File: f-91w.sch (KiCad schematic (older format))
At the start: 41 parts, among them P1 CONN_01X01, P10 CONN_01X01, P11 CONN_01X01, P13 CONN_01X01, P14 CONN_01X01, P2 CONN_01X01, P3 CONN_01X01, P5 CONN_01X01, P6 CONN_01X01, P7 CONN_01X01, P8 CONN_01X01, P9 CONN_01X01, Q1 BC846, U1 CY8C4248LQI-BL483, U2 LCD-F-91W, U3 BME680, Y1 32.768KHz, Y2 24MHz

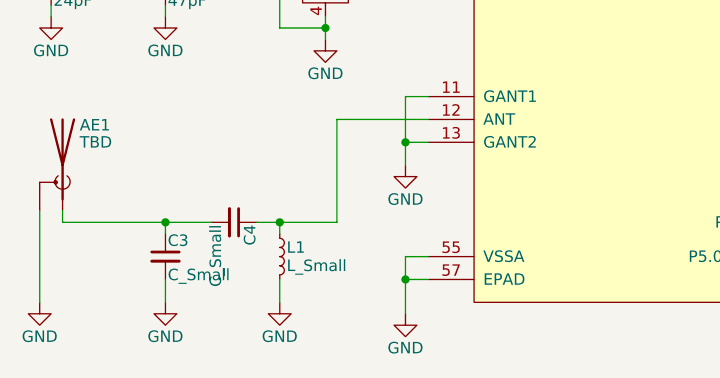
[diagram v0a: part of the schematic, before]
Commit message: Add Johanson 2450AT42E0100 antenna, initial placement
TODO: Proper ground plane and 50R trace
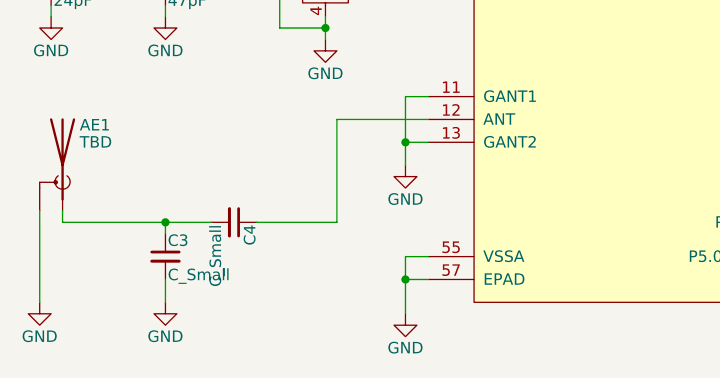
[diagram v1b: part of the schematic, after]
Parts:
- removed L1: L_Small, Resistors_SMD:R_0402, symbol L_Small
- AE1: footprint (none) -> f-91w:2450AT42E0100
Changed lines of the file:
@@
 $EndComp
 $Comp
-L GND #PWR30
+L GND #PWR01
 U 1 1 56EDFDF9
 P 9800 4300
-F 0 "#PWR30" H 9800 4050 50  0001 C CNN
+F 0 "#PWR01" H 9800 4050 50  0001 C CNN
 F 1 "GND" H 9800 4150 50  0000 C CNN
 F 2 "" H 9800 4300 50  0000 C CNN
@@
 $EndComp
 $Comp
-L GND #PWR24
+L GND #PWR02
 U 1 1 56FD3AB4
 P 7000 5050
-F 0 "#PWR24" H 7000 4800 50  0001 C CNN
+F 0 "#PWR02" H 7000 4800 50  0001 C CNN
 F 1 "GND" H 7000 4900 50  0000 C CNN
 F 2 "" H 7000 5050 50  0000 C CNN
@@
 $EndComp
 $Comp
-L VCC #PWR23
+L VCC #PWR03
 U 1 1 570098FF
 P 6550 4550
-F 0 "#PWR23" H 6550 4400 50  0001 C CNN
+F 0 "#PWR03" H 6550 4400 50  0001 C CNN
 F 1 "VCC" H 6550 4700 50  0000 C CNN
 F 2 "" H 6550 4550 50  0000 C CNN
@@
 $EndComp
 $Comp
-L VCC #PWR22
+L VCC #PWR04
 U 1 1 57009B73
 P 6550 4250
-F 0 "#PWR22" H 6550 4100 50  0001 C CNN
+F 0 "#PWR04" H 6550 4100 50  0001 C CNN
 F 1 "VCC" H 6550 4400 50  0000 C CNN
 F 2 "" H 6550 4250 50  0000 C CNN
@@
 B_MODE
 $Comp
-L GND #PWR21
+L GND #PWR05
 U 1 1 5A64BDA3
 P 2750 7550
-F 0 "#PWR21" H 2750 7300 50  0001 C CNN
+F 0 "#PWR05" H 2750 7300 50  0001 C CNN
 F 1 "GND" H 2750 7400 50  0000 C CNN
 F 2 "" H 2750 7550 50  0000 C CNN
@@
 $EndComp
 $Comp
-L GND #PWR20
+L GND #PWR06
 U 1 1 5A64BFB6
 P 2750 6900
-F 0 "#PWR20" H 2750 6650 50  0001 C CNN
+F 0 "#PWR06" H 2750 6650 50  0001 C CNN
 F 1 "GND" H 2750 6750 50  0000 C CNN
 F 2 "" H 2750 6900 50  0000 C CNN
@@
 $EndComp
 $Comp
-L GND #PWR16
+L GND #PWR07
 U 1 1 5A64DCB4
 P 2400 6350
-F 0 "#PWR16" H 2400 6100 50  0001 C CNN
+F 0 "#PWR07" H 2400 6100 50  0001 C CNN
 F 1 "GND" H 2400 6200 50  0000 C CNN
 F 2 "" H 2400 6350 50  0000 C CNN
@@
 $EndComp
 $Comp
-L GND #PWR2
+L GND #PWR08
 U 1 1 5A64E2EF
 P 1200 6250
-F 0 "#PWR2" H 1200 6000 50  0001 C CNN
+F 0 "#PWR08" H 1200 6000 50  0001 C CNN
 F 1 "GND" H 1200 6100 50  0000 C CNN
 F 2 "" H 1200 6250 50  0000 C CNN
@@
 $EndComp
 $Comp
-L GND #PWR6
+L GND #PWR09
 U 1 1 5A64E44A
 P 1700 6250
-F 0 "#PWR6" H 1700 6000 50  0001 C CNN
+F 0 "#PWR09" H 1700 6000 50  0001 C CNN
 F 1 "GND" H 1700 6100 50  0000 C CNN
 F 2 "" H 1700 6250 50  0000 C CNN
@@
 F 0 "AE1" H 1175 7075 50  0000 R CNN
 F 1 "TBD " H 1175 7000 50  0000 R CNN
-F 2 "" H 1250 7000 50  0001 C CNN
+F 2 "f-91w:2450AT42E0100" H 1250 7000 50  0001 C CNN
 F 3 "" H 1250 7000 50  0001 C CNN
 	1    1250 6900
@@
 $EndComp
 $Comp
-L L_Small L1
-U 1 1 5A64F57A
-P 2200 7300
-F 0 "L1" H 2230 7340 50  0000 L CNN
-F 1 "L_Small" H 2230 7260 50  0000 L CNN
-F 2 "Resistors_SMD:R_0402" H 2200 7300 50  0001 C CNN
-F 3 "" H 2200 7300 50  0001 C CNN
-	1    2200 7300
-	1    0    0    -1
-$EndComp
-$Comp
 L C_Small C4
 U 1 1 5A64F666
@@
 $EndComp
 $Comp
-L GND #PWR14
-U 1 1 5A64F863
-P 2200 7500
-F 0 "#PWR14" H 2200 7250 50  0001 C CNN
-F 1 "GND" H 2200 7350 50  0000 C CNN
-F 2 "" H 2200 7500 50  0000 C CNN
-F 3 "" H 2200 7500 50  0000 C CNN
-	1    2200 7500
-	1    0    0    -1
-$EndComp
-$Comp
-L GND #PWR7
+L GND #PWR011
 U 1 1 5A64F8C2
 P 1700 7500
-F 0 "#PWR7" H 1700 7250 50  0001 C CNN
+F 0 "#PWR011" H 1700 7250 50  0001 C CNN
 F 1 "GND" H 1700 7350 50  0000 C CNN
 F 2 "" H 1700 7500 50  0000 C CNN
@@
 $EndComp
 $Comp
-L GND #PWR1
+L GND #PWR012
 U 1 1 5A64FCC4
 P 1150 7500
-F 0 "#PWR1" H 1150 7250 50  0001 C CNN
+F 0 "#PWR012" H 1150 7250 50  0001 C CNN
 F 1 "GND" H 1150 7350 50  0000 C CNN
 F 2 "" H 1150 7500 50  0000 C CNN
@@
 $EndComp
 $Comp
-L GND #PWR15
+L GND #PWR013
 U 1 1 5A650EB4
 P 2250 4650
-F 0 "#PWR15" H 2250 4400 50  0001 C CNN
+F 0 "#PWR013" H 2250 4400 50  0001 C CNN
 F 1 "GND" H 2250 4500 50  0000 C CNN
 F 2 "" H 2250 4650 50  0000 C CNN
@@
 /XRES
 $Comp
-L VDDA #PWR17
+L VDDA #PWR014
 U 1 1 5A652715
 P 2500 3750
-F 0 "#PWR17" H 2500 3600 50  0001 C CNN
+F 0 "#PWR014" H 2500 3600 50  0001 C CNN
 F 1 "VDDA" H 2500 3900 50  0000 C CNN
 F 2 "" H 2500 3750 50  0001 C CNN
@@
 $EndComp
 $Comp
-L GND #PWR28
+L GND #PWR015
 U 1 1 5A6CEE91
 P 8900 1900
-F 0 "#PWR28" H 8900 1650 50  0001 C CNN
+F 0 "#PWR015" H 8900 1650 50  0001 C CNN
 F 1 "GND" H 8900 1750 50  0000 C CNN
 F 2 "" H 8900 1900 50  0000 C CNN
@@
 $EndComp
 $Comp
-L GND #PWR27
+L GND #PWR016
 U 1 1 5A6D0DC3
 P 8550 1900
-F 0 "#PWR27" H 8550 1650 50  0001 C CNN
+F 0 "#PWR016" H 8550 1650 50  0001 C CNN
 F 1 "GND" H 8550 1750 50  0000 C CNN
 F 2 "" H 8550 1900 50  0000 C CNN
@@
 $EndComp
 $Comp
-L GND #PWR26
+L GND #PWR017
 U 1 1 5A6D0E1C
 P 8250 1900
-F 0 "#PWR26" H 8250 1650 50  0001 C CNN
+F 0 "#PWR017" H 8250 1650 50  0001 C CNN
 F 1 "GND" H 8250 1750 50  0000 C CNN
 F 2 "" H 8250 1900 50  0000 C CNN
@@
 $EndComp
 $Comp
-L GND #PWR32
+L GND #PWR018
 U 1 1 5A6D115B
 P 10350 1900
-F 0 "#PWR32" H 10350 1650 50  0001 C CNN
+F 0 "#PWR018" H 10350 1650 50  0001 C CNN
 F 1 "GND" H 10350 1750 50  0000 C CNN
 F 2 "" H 10350 1900 50  0000 C CNN
@@
 SDA
 $Comp
-L VDDD #PWR19
+L VDDD #PWR019
 U 1 1 5A6D21C5
 P 2650 3500
-F 0 "#PWR19" H 2650 3350 50  0001 C CNN
+F 0 "#PWR019" H 2650 3350 50  0001 C CNN
 F 1 "VDDD" H 2650 3650 50  0000 C CNN
 F 2 "" H 2650 3500 50  0001 C CNN
@@
 $EndComp
 $Comp
-L VCC #PWR25
+L VCC #PWR020
 U 1 1 5A6D2B3D
 P 8150 1250
-F 0 "#PWR25" H 8150 1100 50  0001 C CNN
+F 0 "#PWR020" H 8150 1100 50  0001 C CNN
 F 1 "VCC" H 8150 1400 50  0000 C CNN
 F 2 "" H 8150 1250 50  0000 C CNN
@@
 $EndComp
 $Comp
-L VCC #PWR31
+L VCC #PWR021
 U 1 1 5A6D2C66
 P 10350 1250
-F 0 "#PWR31" H 10350 1100 50  0001 C CNN
+F 0 "#PWR021" H 10350 1100 50  0001 C CNN
 F 1 "VCC" H 10350 1400 50  0000 C CNN
 F 2 "" H 10350 1250 50  0000 C CNN
@@
 $EndComp
 $Comp
-L VDDR #PWR18
+L VDDR #PWR022
 U 1 1 5A652763
 P 2500 4050
-F 0 "#PWR18" H 2500 3900 50  0001 C CNN
+F 0 "#PWR022" H 2500 3900 50  0001 C CNN
 F 1 "VDDR" H 2500 4200 50  0000 C CNN
 F 2 "" H 2500 4050 50  0001 C CNN
@@
 $EndComp
 $Comp
-L VDDR #PWR12
+L VDDR #PWR023
 U 1 1 5A6DCCF0
 P 1900 2700
-F 0 "#PWR12" H 1900 2550 50  0001 C CNN
+F 0 "#PWR023" H 1900 2550 50  0001 C CNN
 F 1 "VDDR" H 1900 2850 50  0000 C CNN
 F 2 "" H 1900 2700 50  0001 C CNN
@@
 $EndComp
 $Comp
-L GND #PWR13
+L GND #PWR024
 U 1 1 5A6DCDD7
 P 1900 3300
-F 0 "#PWR13" H 1900 3050 50  0001 C CNN
+F 0 "#PWR024" H 1900 3050 50  0001 C CNN
 F 1 "GND" H 1900 3150 50  0000 C CNN
 F 2 "" H 1900 3300 50  0000 C CNN
@@
 $EndComp
 $Comp
-L VDDA #PWR10
+L VDDA #PWR025
 U 1 1 5A6DE047
 P 1900 1950
-F 0 "#PWR10" H 1900 1800 50  0001 C CNN
+F 0 "#PWR025" H 1900 1800 50  0001 C CNN
 F 1 "VDDA" H 1900 2100 50  0000 C CNN
 F 2 "" H 1900 1950 50  0001 C CNN
@@
 $EndComp
 $Comp
-L VDDD #PWR8
+L VDDD #PWR026
 U 1 1 5A6DE0AF
 P 1900 1150
-F 0 "#PWR8" H 1900 1000 50  0001 C CNN
+F 0 "#PWR026" H 1900 1000 50  0001 C CNN
 F 1 "VDDD" H 1900 1300 50  0000 C CNN
 F 2 "" H 1900 1150 50  0001 C CNN
@@
 $EndComp
 $Comp
-L GND #PWR11
+L GND #PWR027
 U 1 1 5A6DE772
 P 1900 2250
-F 0 "#PWR11" H 1900 2000 50  0001 C CNN
+F 0 "#PWR027" H 1900 2000 50  0001 C CNN
 F 1 "GND" H 1900 2100 50  0000 C CNN
 F 2 "" H 1900 2250 50  0000 C CNN
@@
 $EndComp
 $Comp
-L GND #PWR9
+L GND #PWR028
 U 1 1 5A6DE7EC
 P 1900 1500
-F 0 "#PWR9" H 1900 1250 50  0001 C CNN
+F 0 "#PWR028" H 1900 1250 50  0001 C CNN
 F 1 "GND" H 1900 1350 50  0000 C CNN
 F 2 "" H 1900 1500 50  0000 C CNN
@@
 $EndComp
 $Comp
-L VCC #PWR3
+L VCC #PWR029
 U 1 1 5A6E1864
 P 1450 1100
-F 0 "#PWR3" H 1450 950 50  0001 C CNN
+F 0 "#PWR029" H 1450 950 50  0001 C CNN
 F 1 "VCC" H 1450 1250 50  0000 C CNN
 F 2 "" H 1450 1100 50  0000 C CNN
@@
 $EndComp
 $Comp
-L VCC #PWR4
+L VCC #PWR030
 U 1 1 5A6E1A5B
 P 1450 1900
-F 0 "#PWR4" H 1450 1750 50  0001 C CNN
+F 0 "#PWR030" H 1450 1750 50  0001 C CNN
 F 1 "VCC" H 1450 2050 50  0000 C CNN
 F 2 "" H 1450 1900 50  0000 C CNN
@@
 $EndComp
 $Comp
-L VCC #PWR5
+L VCC #PWR031
 U 1 1 5A6E1C7D
 P 1450 2750
-F 0 "#PWR5" H 1450 2600 50  0001 C CNN
+F 0 "#PWR031" H 1450 2600 50  0001 C CNN
 F 1 "VCC" H 1450 2900 50  0000 C CNN
 F 2 "" H 1450 2750 50  0000 C CNN
@@
 BUZ_EN
 $Comp
-L VCC #PWR29
+L VCC #PWR032
 U 1 1 5A6E93F9
 P 9550 4850
-F 0 "#PWR29" H 9550 4700 50  0001 C CNN
+F 0 "#PWR032" H 9550 4700 50  0001 C CNN
 F 1 "VCC" H 9550 5000 50  0000 C CNN
 F 2 "" H 9550 4850 50  0000 C CNN
@@
 	2450 7150 2100 7150
 Wire Wire Line
-	2200 7150 2200 7200
-Connection ~ 2200 7150
-Wire Wire Line
 	1700 7500 1700 7400
 Wire Wire Line
@@
 	1700 7150 1700 7200
 Wire Wire Line
-	2200 7400 2200 7500
-Wire Wire Line
 	1250 7150 1250 7100

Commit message: Add test points for SWD interface
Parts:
- P1, P2, P3: footprint (none) -> f-91w:TP_1.2mm
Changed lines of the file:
@@
 F 0 "P1" H 8700 5650 50  0000 C CNN
 F 1 "CONN_01X01" H 9000 5550 50  0000 C CNN
-F 2 "" H 8700 5550 50  0001 C CNN
+F 2 "f-91w:TP_1.2mm" H 8700 5550 50  0001 C CNN
 F 3 "" H 8700 5550 50  0000 C CNN
 	1    8700 5550
@@
 F 0 "P2" H 8700 5950 50  0000 C CNN
 F 1 "CONN_01X01" H 9000 5850 50  0000 C CNN
-F 2 "" H 8700 5850 50  0001 C CNN
+F 2 "f-91w:TP_1.2mm" H 8700 5850 50  0001 C CNN
 F 3 "" H 8700 5850 50  0000 C CNN
 	1    8700 5850
@@
 F 0 "P3" H 8700 6250 50  0000 C CNN
 F 1 "CONN_01X01" H 9000 6150 50  0000 C CNN
-F 2 "" H 8700 6150 50  0001 C CNN
+F 2 "f-91w:TP_1.2mm" H 8700 6150 50  0001 C CNN
 F 3 "" H 8700 6150 50  0000 C CNN
 	1    8700 6150

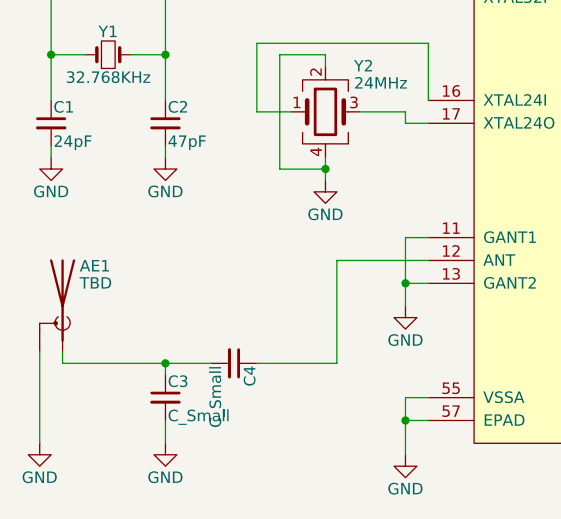
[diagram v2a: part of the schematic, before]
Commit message: Update antenna footprint to add polarity markings
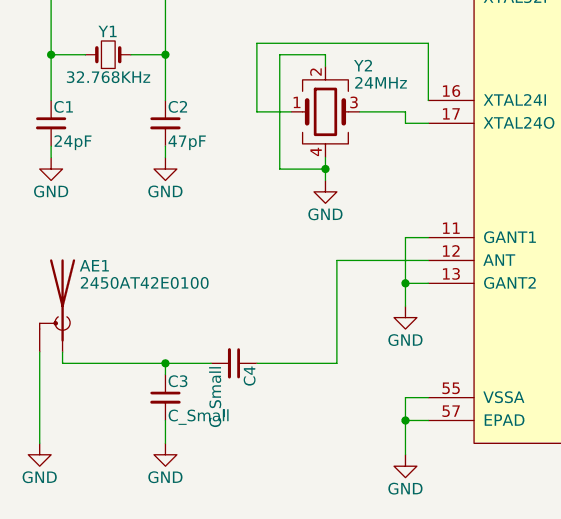
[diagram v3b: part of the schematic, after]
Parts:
- AE1: value TBD -> 2450AT42E0100
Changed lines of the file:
@@
 P 1250 6900
 F 0 "AE1" H 1175 7075 50  0000 R CNN
-F 1 "TBD " H 1175 7000 50  0000 R CNN
+F 1 "2450AT42E0100" H 1175 7000 50  0000 R CNN
 F 2 "f-91w:2450AT42E0100" H 1250 7000 50  0001 C CNN
 F 3 "" H 1250 7000 50  0001 C CNN
@@
 $EndComp
 $Comp
-L GND #PWR011
+L GND #PWR010
 U 1 1 5A64F8C2
 P 1700 7500
-F 0 "#PWR011" H 1700 7250 50  0001 C CNN
+F 0 "#PWR010" H 1700 7250 50  0001 C CNN
 F 1 "GND" H 1700 7350 50  0000 C CNN
 F 2 "" H 1700 7500 50  0000 C CNN
@@
 $EndComp
 $Comp
-L GND #PWR012
+L GND #PWR011
 U 1 1 5A64FCC4
 P 1150 7500
-F 0 "#PWR012" H 1150 7250 50  0001 C CNN
+F 0 "#PWR011" H 1150 7250 50  0001 C CNN
 F 1 "GND" H 1150 7350 50  0000 C CNN
 F 2 "" H 1150 7500 50  0000 C CNN
@@
 $EndComp
 $Comp
-L GND #PWR013
+L GND #PWR012
 U 1 1 5A650EB4
 P 2250 4650
-F 0 "#PWR013" H 2250 4400 50  0001 C CNN
+F 0 "#PWR012" H 2250 4400 50  0001 C CNN
 F 1 "GND" H 2250 4500 50  0000 C CNN
 F 2 "" H 2250 4650 50  0000 C CNN
@@
 /XRES
 $Comp
-L VDDA #PWR014
+L VDDA #PWR013
 U 1 1 5A652715
 P 2500 3750
-F 0 "#PWR014" H 2500 3600 50  0001 C CNN
+F 0 "#PWR013" H 2500 3600 50  0001 C CNN
 F 1 "VDDA" H 2500 3900 50  0000 C CNN
 F 2 "" H 2500 3750 50  0001 C CNN
@@
 $EndComp
 $Comp
-L GND #PWR015
+L GND #PWR014
 U 1 1 5A6CEE91
 P 8900 1900
-F 0 "#PWR015" H 8900 1650 50  0001 C CNN
+F 0 "#PWR014" H 8900 1650 50  0001 C CNN
 F 1 "GND" H 8900 1750 50  0000 C CNN
 F 2 "" H 8900 1900 50  0000 C CNN
@@
 $EndComp
 $Comp
-L GND #PWR016
+L GND #PWR015
 U 1 1 5A6D0DC3
 P 8550 1900
-F 0 "#PWR016" H 8550 1650 50  0001 C CNN
+F 0 "#PWR015" H 8550 1650 50  0001 C CNN
 F 1 "GND" H 8550 1750 50  0000 C CNN
 F 2 "" H 8550 1900 50  0000 C CNN
@@
 $EndComp
 $Comp
-L GND #PWR017
+L GND #PWR016
 U 1 1 5A6D0E1C
 P 8250 1900
-F 0 "#PWR017" H 8250 1650 50  0001 C CNN
+F 0 "#PWR016" H 8250 1650 50  0001 C CNN
 F 1 "GND" H 8250 1750 50  0000 C CNN
 F 2 "" H 8250 1900 50  0000 C CNN
@@
 $EndComp
 $Comp
-L GND #PWR018
+L GND #PWR017
 U 1 1 5A6D115B
 P 10350 1900
-F 0 "#PWR018" H 10350 1650 50  0001 C CNN
+F 0 "#PWR017" H 10350 1650 50  0001 C CNN
 F 1 "GND" H 10350 1750 50  0000 C CNN
 F 2 "" H 10350 1900 50  0000 C CNN
@@
 SDA
 $Comp
-L VDDD #PWR019
+L VDDD #PWR018
 U 1 1 5A6D21C5
 P 2650 3500
-F 0 "#PWR019" H 2650 3350 50  0001 C CNN
+F 0 "#PWR018" H 2650 3350 50  0001 C CNN
 F 1 "VDDD" H 2650 3650 50  0000 C CNN
 F 2 "" H 2650 3500 50  0001 C CNN
@@
 $EndComp
 $Comp
-L VCC #PWR020
+L VCC #PWR019
 U 1 1 5A6D2B3D
 P 8150 1250
-F 0 "#PWR020" H 8150 1100 50  0001 C CNN
+F 0 "#PWR019" H 8150 1100 50  0001 C CNN
 F 1 "VCC" H 8150 1400 50  0000 C CNN
 F 2 "" H 8150 1250 50  0000 C CNN
@@
 $EndComp
 $Comp
-L VCC #PWR021
+L VCC #PWR020
 U 1 1 5A6D2C66
 P 10350 1250
-F 0 "#PWR021" H 10350 1100 50  0001 C CNN
+F 0 "#PWR020" H 10350 1100 50  0001 C CNN
 F 1 "VCC" H 10350 1400 50  0000 C CNN
 F 2 "" H 10350 1250 50  0000 C CNN
@@
 $EndComp
 $Comp
-L VDDR #PWR022
+L VDDR #PWR021
 U 1 1 5A652763
 P 2500 4050
-F 0 "#PWR022" H 2500 3900 50  0001 C CNN
+F 0 "#PWR021" H 2500 3900 50  0001 C CNN
 F 1 "VDDR" H 2500 4200 50  0000 C CNN
 F 2 "" H 2500 4050 50  0001 C CNN
@@
 $EndComp
 $Comp
-L VDDR #PWR023
+L VDDR #PWR022
 U 1 1 5A6DCCF0
 P 1900 2700
-F 0 "#PWR023" H 1900 2550 50  0001 C CNN
+F 0 "#PWR022" H 1900 2550 50  0001 C CNN
 F 1 "VDDR" H 1900 2850 50  0000 C CNN
 F 2 "" H 1900 2700 50  0001 C CNN
@@
 $EndComp
 $Comp
-L GND #PWR024
+L GND #PWR023
 U 1 1 5A6DCDD7
 P 1900 3300
-F 0 "#PWR024" H 1900 3050 50  0001 C CNN
+F 0 "#PWR023" H 1900 3050 50  0001 C CNN
 F 1 "GND" H 1900 3150 50  0000 C CNN
 F 2 "" H 1900 3300 50  0000 C CNN
@@
 $EndComp
 $Comp
-L VDDA #PWR025
+L VDDA #PWR024
 U 1 1 5A6DE047
 P 1900 1950
-F 0 "#PWR025" H 1900 1800 50  0001 C CNN
+F 0 "#PWR024" H 1900 1800 50  0001 C CNN
 F 1 "VDDA" H 1900 2100 50  0000 C CNN
 F 2 "" H 1900 1950 50  0001 C CNN
@@
 $EndComp
 $Comp
-L VDDD #PWR026
+L VDDD #PWR025
 U 1 1 5A6DE0AF
 P 1900 1150
-F 0 "#PWR026" H 1900 1000 50  0001 C CNN
+F 0 "#PWR025" H 1900 1000 50  0001 C CNN
 F 1 "VDDD" H 1900 1300 50  0000 C CNN
 F 2 "" H 1900 1150 50  0001 C CNN
@@
 $EndComp
 $Comp
-L GND #PWR027
+L GND #PWR026
 U 1 1 5A6DE772
 P 1900 2250
-F 0 "#PWR027" H 1900 2000 50  0001 C CNN
+F 0 "#PWR026" H 1900 2000 50  0001 C CNN
 F 1 "GND" H 1900 2100 50  0000 C CNN
 F 2 "" H 1900 2250 50  0000 C CNN
@@
 $EndComp
 $Comp
-L GND #PWR028
+L GND #PWR027
 U 1 1 5A6DE7EC
 P 1900 1500
-F 0 "#PWR028" H 1900 1250 50  0001 C CNN
+F 0 "#PWR027" H 1900 1250 50  0001 C CNN
 F 1 "GND" H 1900 1350 50  0000 C CNN
 F 2 "" H 1900 1500 50  0000 C CNN
@@
 $EndComp
 $Comp
-L VCC #PWR029
+L VCC #PWR028
 U 1 1 5A6E1864
 P 1450 1100
-F 0 "#PWR029" H 1450 950 50  0001 C CNN
+F 0 "#PWR028" H 1450 950 50  0001 C CNN
 F 1 "VCC" H 1450 1250 50  0000 C CNN
 F 2 "" H 1450 1100 50  0000 C CNN
@@
 $EndComp
 $Comp
-L VCC #PWR030
+L VCC #PWR029
 U 1 1 5A6E1A5B
 P 1450 1900
-F 0 "#PWR030" H 1450 1750 50  0001 C CNN
+F 0 "#PWR029" H 1450 1750 50  0001 C CNN
 F 1 "VCC" H 1450 2050 50  0000 C CNN
 F 2 "" H 1450 1900 50  0000 C CNN
@@
 $EndComp
 $Comp
-L VCC #PWR031
+L VCC #PWR030
 U 1 1 5A6E1C7D
 P 1450 2750
-F 0 "#PWR031" H 1450 2600 50  0001 C CNN
+F 0 "#PWR030" H 1450 2600 50  0001 C CNN
 F 1 "VCC" H 1450 2900 50  0000 C CNN
 F 2 "" H 1450 2750 50  0000 C CNN
@@
 BUZ_EN
 $Comp
-L VCC #PWR032
+L VCC #PWR031
 U 1 1 5A6E93F9
 P 9550 4850
-F 0 "#PWR032" H 9550 4700 50  0001 C CNN
+F 0 "#PWR031" H 9550 4700 50  0001 C CNN
 F 1 "VCC" H 9550 5000 50  0000 C CNN
 F 2 "" H 9550 4850 50  0000 C CNN

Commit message: Fix 32KHz crystal footprint for Abracon ABS06 series
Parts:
- Y1: footprint Crystals:Crystal_SMD_TXC_9HT11-2pin_2.0x1.2mm -> f-91w:Crystal_SMD_Abracon_ABS06-2pin_2.0x1.2mm
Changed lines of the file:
@@
 F 0 "Y1" H 1450 5900 50  0000 C CNN
 F 1 "32.768KHz" H 1450 5700 50  0000 C CNN
-F 2 "Crystals:Crystal_SMD_TXC_9HT11-2pin_2.0x1.2mm" H 1450 5800 50  0001 C CNN
+F 2 "f-91w:Crystal_SMD_Abracon_ABS06-2pin_2.0x1.2mm" H 1450 5800 50  0001 C CNN
 F 3 "" H 1450 5800 50  0001 C CNN
 F 4 "ABS06-32.768KHZ-1-T" H 1450 5800 60  0001 C CNN "MPN"

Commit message: Update schematic and project to KiCad 5.0
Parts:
- AE1: symbol Antenna_Shield -> Device:Antenna_Shield
- C1, C10, C11, C12, C13, C14, C15, C16, C17, C18, C2, C3, C4, C5, C6, C7, C8, C9: symbol C_Small -> Device:C_Small
- L4: symbol Ferrite_Bead_Small -> Device:Ferrite_Bead_Small
- P1, P10, P11, P13, P14, P2, P3, P5, P6, P7, P8, P9: symbol Conn_01x01 -> Connector_Generic:Conn_01x01
- Q1: symbol Q_NPN_BEC -> Device:Q_NPN_BEC
- R2, R3: symbol R -> Device:R
- U1: symbol CY8C4248LQI-BL483 -> f-91w:CY8C4248LQI-BL483
- U2: symbol LCD-F-91W -> f-91w:LCD-F-91W
- U3: symbol BME680 -> f-91w:BME680
- Y1: symbol Crystal_Small -> Device:Crystal_Small
- Y2: symbol Crystal_GND24 -> Device:Crystal_GND24

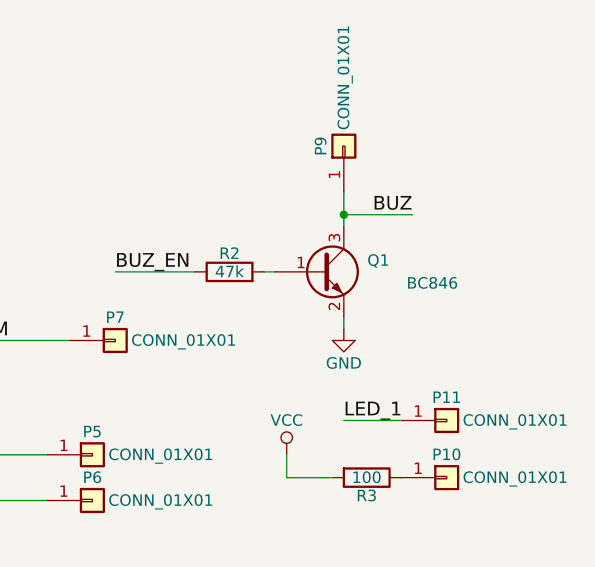
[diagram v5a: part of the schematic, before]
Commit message: Change Q1 from obsolete BC846 to BC847BTT1
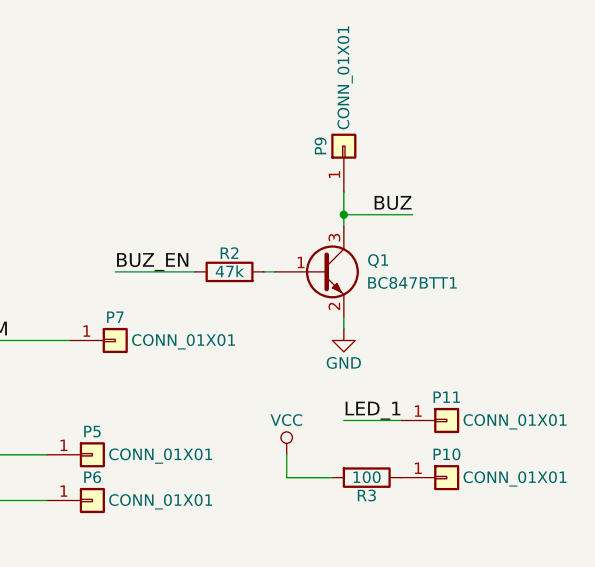
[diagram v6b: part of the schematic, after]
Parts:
- Q1: value BC846 -> BC847BTT1
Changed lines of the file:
@@
 P 9700 4050
 F 0 "Q1" H 10000 4100 50  0000 R CNN
-F 1 "BC846" H 10300 4000 50  0000 R CNN
+F 1 "BC847BTT1" H 10300 4000 50  0000 R CNN
 F 2 "f-91w:SOT416" H 9900 4150 50  0001 C CNN
 F 3 "" H 9700 4050 50  0000 C CNN
